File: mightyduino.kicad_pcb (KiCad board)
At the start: 2 copper layers, 46.2 x 23.1 mm, 24 parts, among them IC1 ATMEGA644P-A, P1 CONN_01X18, P2 CONN_01X06, P3 CONN_01X18, SW1 RESET, U1 MIC5219-3.3YM5, X1 CSTCE 16MHZ

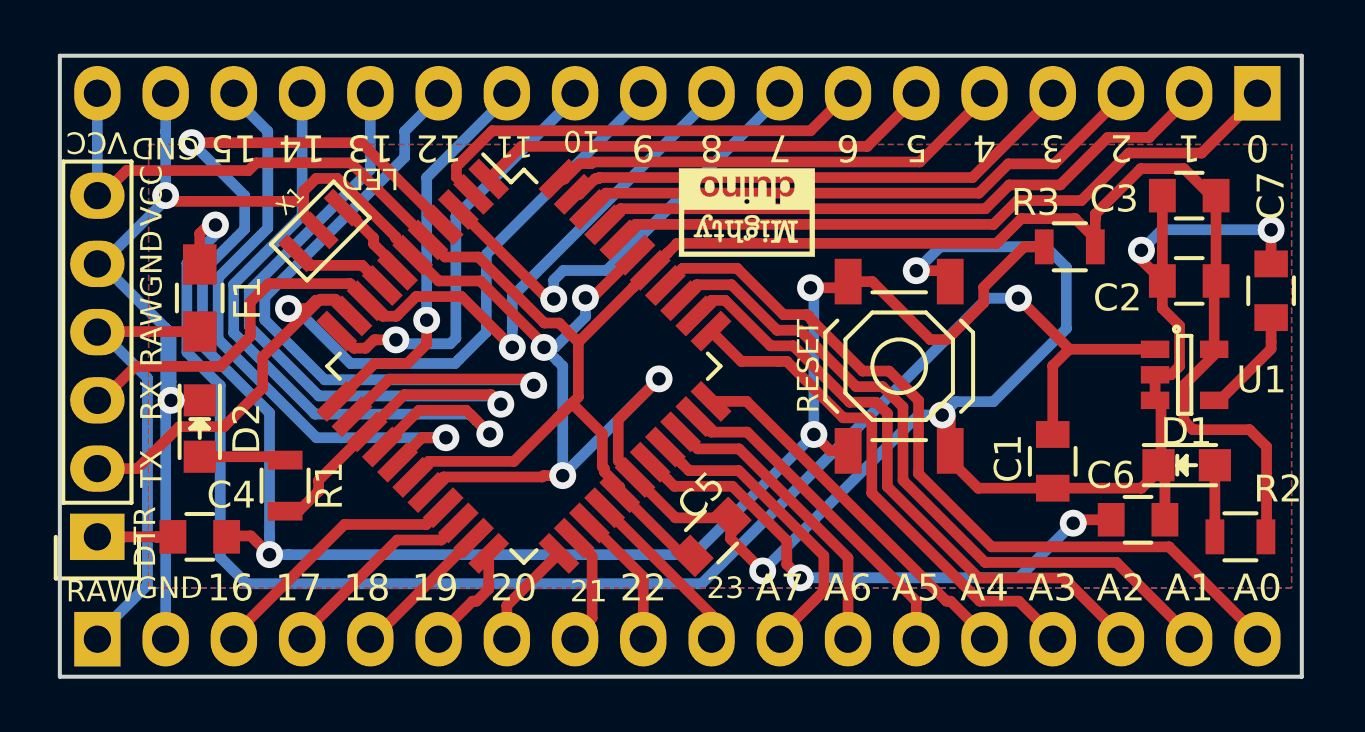
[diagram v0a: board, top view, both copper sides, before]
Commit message: switched led from d13 to d0, cosmetic improvments
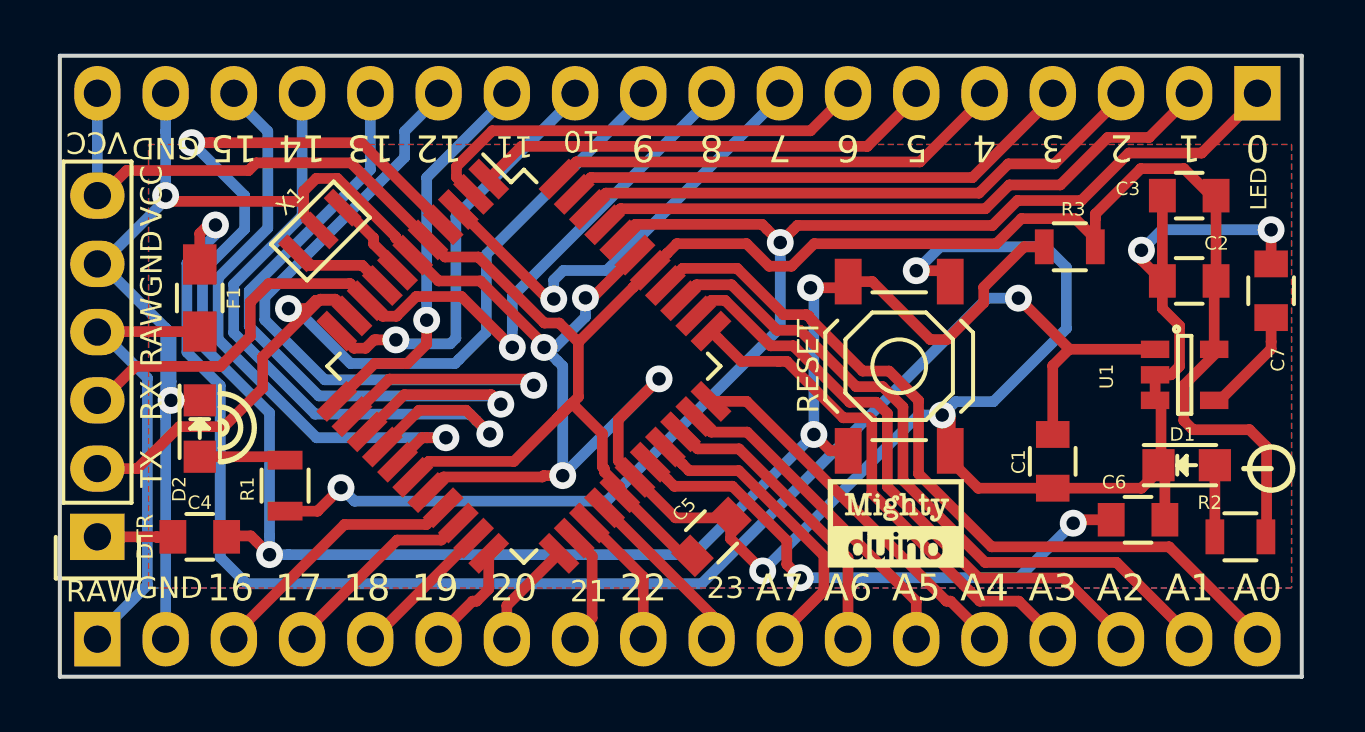
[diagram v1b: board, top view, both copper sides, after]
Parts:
- removed the G*** at (160.0, 116.2)
- removed REF**: Symbol_OSHW-Logo_SilkScreen, Symbols:Symbol_OSHW-Logo_SilkScreen
- added G***: LOGO, parts:dev76logo, B.Cu at (161.3, 115.6)
- added G***: LOGO, parts:logo_oshw, B.Cu at (163.6, 113.8)
- added G***: LOGO, parts:specs, B.Cu at (157.2, 110.5)
- moved G*** 12.8 mm to (159.3, 116.3), turned to 0 degrees
- moved G*** 0.52 mm to (168.9, 110.5)
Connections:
- R1 pad 2: /D13 -> /D0
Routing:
- net /D0: track 26.1 -> 52.0 mm, vias 0 -> 2
- net /D13: track 31.3 -> 26.8 mm
- net VCC: track 87.7 -> 88.4 mm
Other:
- board text added: "v1.1"
- board text removed: "v1.0"

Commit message: updated ressonator 3d design
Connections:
- U1 pad 3: GND -> Net-(C1-Pad1)
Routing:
- net GND: track 134.5 -> 130.9 mm
- net Net-(C1-Pad1): track 59.2 -> 62.2 mm
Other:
- board text added: "v1.2"
- board text removed: "v1.1"
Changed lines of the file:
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@@
     (thickness 1.6)
     (drawings 108)
-    (tracks 526)
+    (tracks 527)
     (zones 0)
     (modules 25)
@@
   (title_block
     (title Mightyduino)
-    (date 2016-12-07)
-    (rev 1.1)
+    (date 2016-12-09)
+    (rev 1.2)
     (company dev76.org)
   )
@@
     (pad 1 smd rect (at -1.2 -0.0365 225) (size 0.5 1.5) (layers F.Cu F.Paste F.Mask)
       (net 13 "Net-(IC1-Pad7)"))
-    (model /Users/paulo/MEOCloud/kicad/mightyduino/3d/cstce.wrl
-      (at (xyz -0.055 -0.02 0))
+    (model /Users/paulo/MEOCloud/kicad/mightyduino/cstce4.wrl
+      (at (xyz 0.06 0.025 0))
       (scale (xyz 0.39 0.39 0.39))
-      (rotate (xyz 0 0 0))
+      (rotate (xyz -90 0 0))
     )
   )
@@
       (net 2 GND))
     (pad 3 smd rect (at -1.1 0.95) (size 1.06 0.65) (layers F.Cu F.Paste F.Mask)
-      (net 2 GND))
+      (net 1 "Net-(C1-Pad1)"))
     (pad 4 smd rect (at 1.1 0.95) (size 1.06 0.65) (layers F.Cu F.Paste F.Mask)
       (net 44 "Net-(C7-Pad1)"))
@@
   (gr_arc (start 134.112 112.776) (end 134.112 112.014) (angle 180) (layer F.SilkS) (width 0.2))
   (gr_arc (start 134.112 112.776) (end 134.112 112.522) (angle 161.5650512) (layer F.SilkS) (width 0.2))
-  (gr_text v1.1 (at 173.355 116.205 90) (layer B.SilkS)
+  (gr_text v1.2 (at 173.355 116.205 90) (layer B.SilkS)
     (effects (font (size 0.8 0.8) (thickness 0.2)) (justify mirror))
   )
@@
   )
   (segment (start 157.48 107.442) (end 157.48 114.046) (width 0.4) (layer Dwgs.User) (net 0))
+  (segment (start 168.91 109.86) (end 167.64 109.86) (width 0.4) (layer F.Cu) (net 1))
+  (segment (start 167.64 109.86) (end 165.71 109.86) (width 0.4) (layer F.Cu) (net 1))
+  (segment (start 168.91 111.76) (end 167.98 111.76) (width 0.4) (layer F.Cu) (net 1))
+  (segment (start 167.98 111.76) (end 167.64 111.42) (width 0.4) (layer F.Cu) (net 1))
+  (segment (start 167.64 111.42) (end 167.64 109.86) (width 0.4) (layer F.Cu) (net 1))
   (segment (start 165.71 109.86) (end 165.71 109.843636) (width 0.4) (layer F.Cu) (net 1))
   (segment (start 165.71 109.843636) (end 163.822829 107.956465) (width 0.4) (layer F.Cu) (net 1))
   (segment (start 165.1 113.03) (end 165.1 110.47) (width 0.4) (layer F.Cu) (net 1))
-  (segment (start 168.91 109.86) (end 165.71 109.86) (width 0.4) (layer F.Cu) (net 1))
   (segment (start 165.71 109.86) (end 165.1 110.47) (width 0.4) (layer F.Cu) (net 1))
   (segment (start 134.112 111.207296) (end 132.872511 109.967808) (width 0.4) (layer B.Cu) (net 1))
@@
   (segment (start 169.18 108.34) (end 169.18 107.315) (width 0.4) (layer F.Cu) (net 2))
   (segment (start 169.18 107.315) (end 169.18 104.14) (width 0.4) (layer F.Cu) (net 2))
-  (segment (start 168.91 110.81) (end 168.91 111.76) (width 0.4) (layer F.Cu) (net 2))
-  (segment (start 169.13098 114.3) (end 169.13098 111.98098) (width 0.4) (layer F.Cu) (net 2))
-  (segment (start 169.13098 111.98098) (end 168.91 111.76) (width 0.4) (layer F.Cu) (net 2))
   (segment (start 165.1 115.03) (end 168.40098 115.03) (width 0.4) (layer F.Cu) (net 2))
   (segment (start 132.08 104.14) (end 132.08 104.163688) (width 0.4) (layer B.Cu) (net 2))

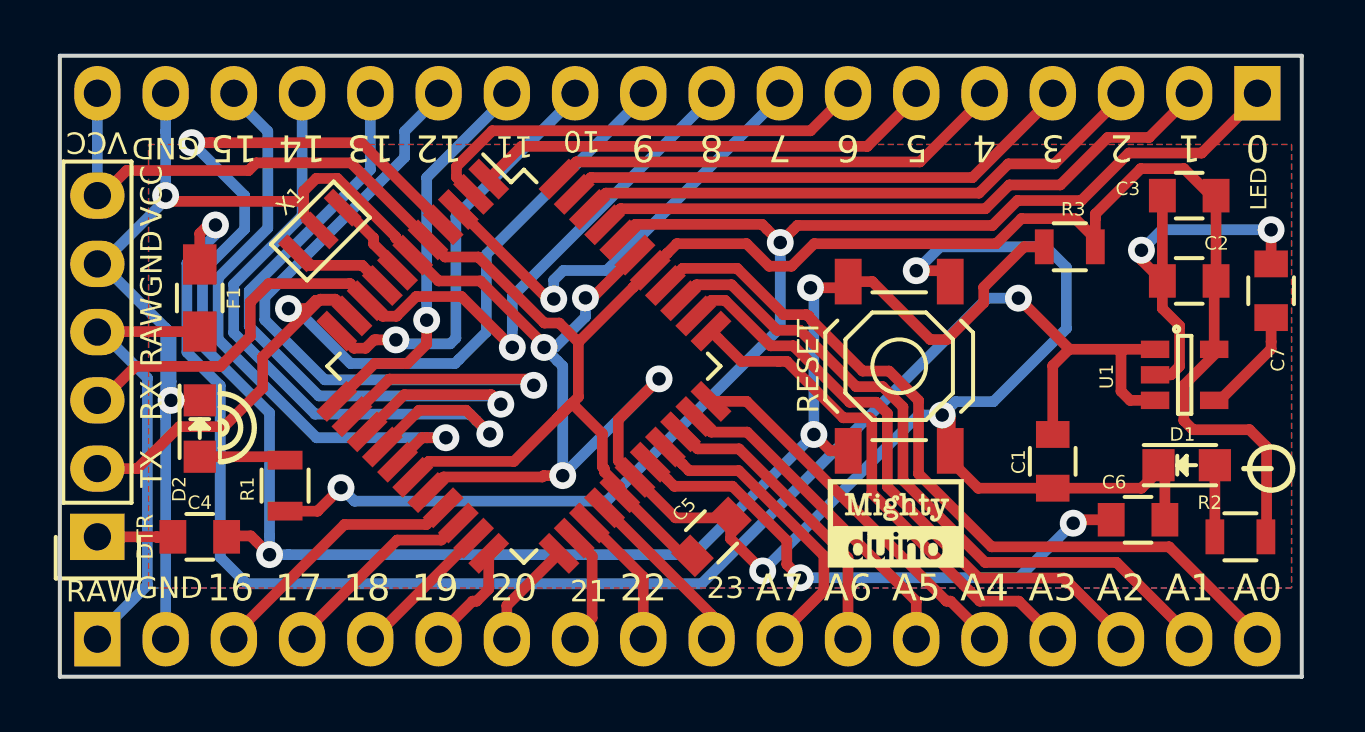
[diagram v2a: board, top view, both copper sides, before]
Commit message: C1,C3 better footprint, added RESET PIN
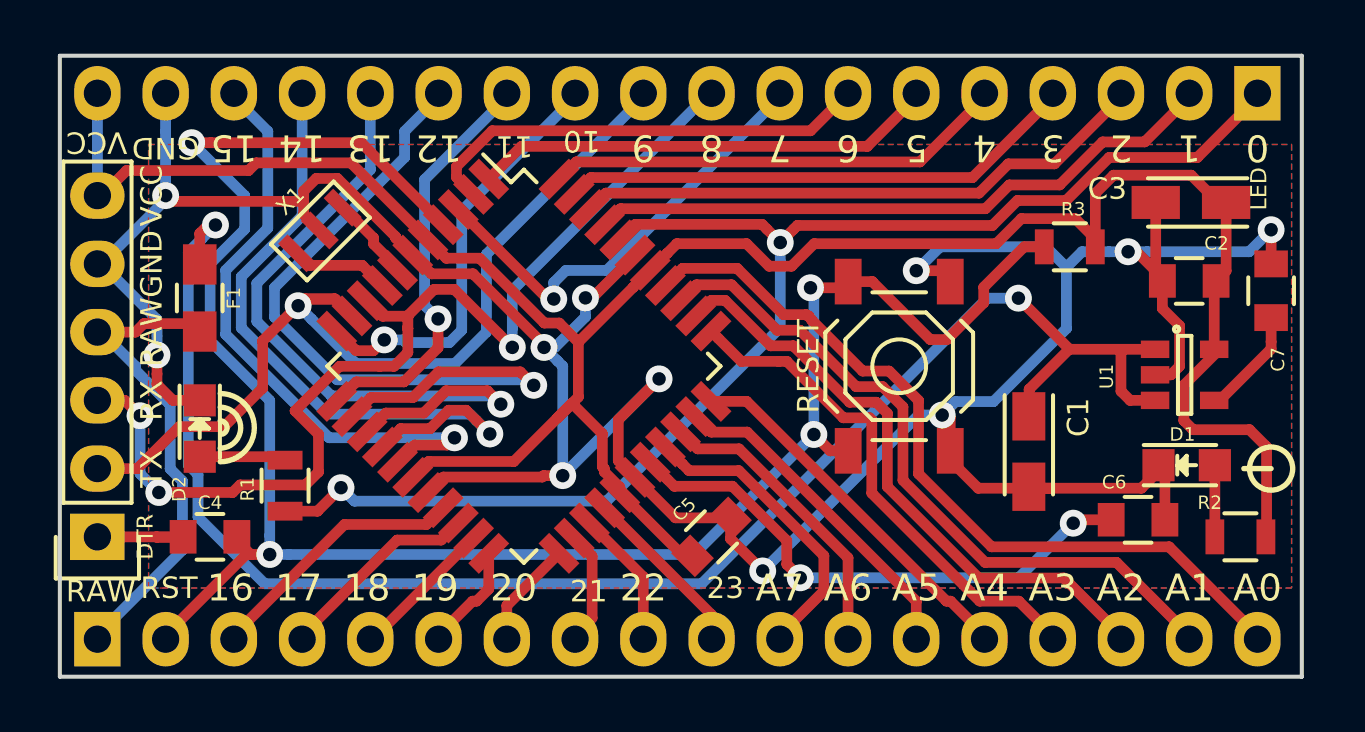
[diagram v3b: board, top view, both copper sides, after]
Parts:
- removed the G*** at (159.3, 116.3)
- C1, C3: footprint Capacitors_SMD:C_0805 -> Capacitors_Tantalum_SMD:TantalC_SizeA_EIA-3216_Reflow
- moved C1 0.96 mm to (164.2, 113.7)
- moved C4 0.38 mm to (133.7, 116.8)
- moved C3 0.26 mm to (170.2, 104.4)
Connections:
- P3 pad 2: GND -> /RESET
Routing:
- net GND: track 130.9 -> 122.9 mm
- net /D8: track 32.1 -> 40.1 mm, vias 1 -> 3
- net /RESET: track 70.9 -> 75.0 mm
- net /RAW: track 17.3 -> 18.7 mm
- net Net-(C1-Pad1): track 62.2 -> 61.3 mm
- net /D11: track 14.8 -> 15.5 mm
- net VCC: track 88.4 -> 89.0 mm
- net /D14: track 26.0 -> 25.5 mm
- net /DTR: track 3.49 -> 3.99 mm
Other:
- board text added: "2017 Dev76.org"
- board text added: "RST"
- board text added: "v1.3"
- board text removed: "2016 Dev76.org"
- board text removed: "v1.2"
